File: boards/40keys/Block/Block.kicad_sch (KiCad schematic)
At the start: 196 parts, among them J1 Conn_01x08_Female, J1 Conn_01x12_Female, J2 Conn_01x12_Female, J3 Conn_01x12_Female, J4 Conn_01x08_Female, J6 Conn_01x12_Female, SW1 SW_Push, SW10 SW_Push, SW11 SW_Push, SW12 SW_Push, SW13 SW_Push, SW14 SW_Push, SW15 SW_Push, SW16 SW_Push, SW17 SW_Push, SW18 SW_Push, SW19 SW_Push, SW2 SW_Push, SW20 SW_Push, SW21 SW_Push, SW22 SW_Push, SW23 SW_Push, SW24 SW_Push, SW25 SW_Push, SW26 SW_Push, SW27 SW_Push, SW28 SW_Push, SW29 SW_Push, SW3 SW_Push, SW30 SW_Push, SW31 SW_Push, SW32 SW_Push, SW33 SW_Push, SW34 SW_Push, SW35 SW_Push, SW36 RotaryEncoder, SW36 Rotary_Encoder_Switch, SW37 SW_SPDT, SW38 SW_Push, SW39 SW_Push, SW4 SW_Push, SW40 SW_Push, SW41 SW_Push, SW42 SW_Push, SW43 SW_Push, SW44 SW_Push, SW45 SW_Push, SW46 SW_Push, SW5 SW_Push, SW6 SW_Push, SW7 SW_Push, SW8 SW_Push, SW9 SW_Push, U1 Elite-C, U2 74HC595, U3 TCR2EF19,LM(CT, U4 PMW3360DM-T2QU, U5 DRV2605L, U6 74LVC1T45

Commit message: block routed and jlc files
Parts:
- removed JP2: SolderJumper_3_Open, Jumper:SolderJumper-3_P1.3mm_Open_RoundedPad1.0x1.5mm_NumberLabels, symbol Jumper:SolderJumper_3_Open
- D1, D10, D11, D12, D13, D14, D15, D16, D17, D18, D19, D2, D20, D21, D22, D23, D24, D25, D26, D27, D28, D29, D3, D30, D31, D32, D33, D34, D4, D43, D5, D6, D7, D75, D76, D77, D78, D79, D8, D80, D81, D82, D9: footprint Diode_SMD:D_SOD-123 -> Alaa:D_SOD-123-rotated
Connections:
- net GPIO27 is gone; now on net EncR_1: U1.18 (A1/PF6)
- net GPIO16: now also JP3.2 (C)
- net LED_3V3: now also U1.28 (F1)
- net MOTION: now also JP3.3 (B); no longer U1.28 (F1)
- net NCS_2: now also U1.13 (10/PB6); no longer JP3.3 (B)
- removed net GPIO15: JP3.2 (C), U1.13 (10/PB6)

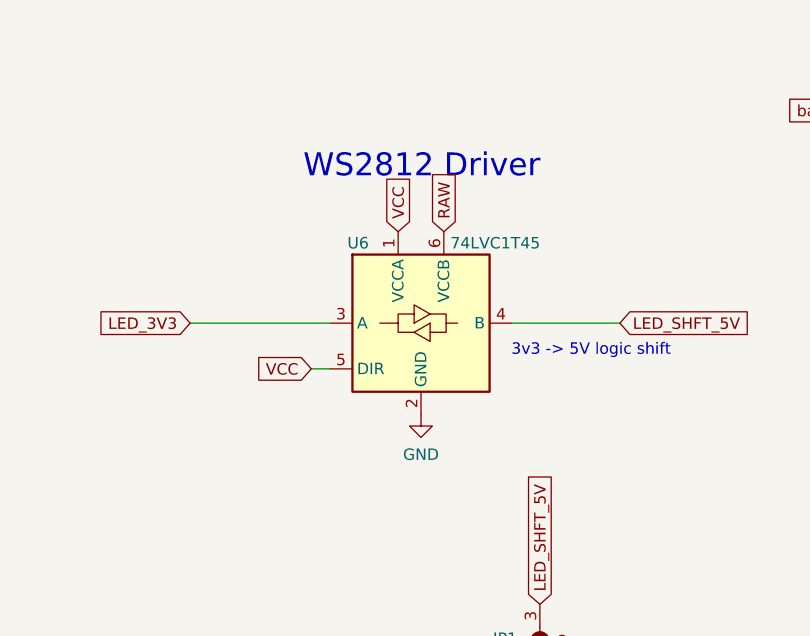
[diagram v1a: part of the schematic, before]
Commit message: block updated level shifter
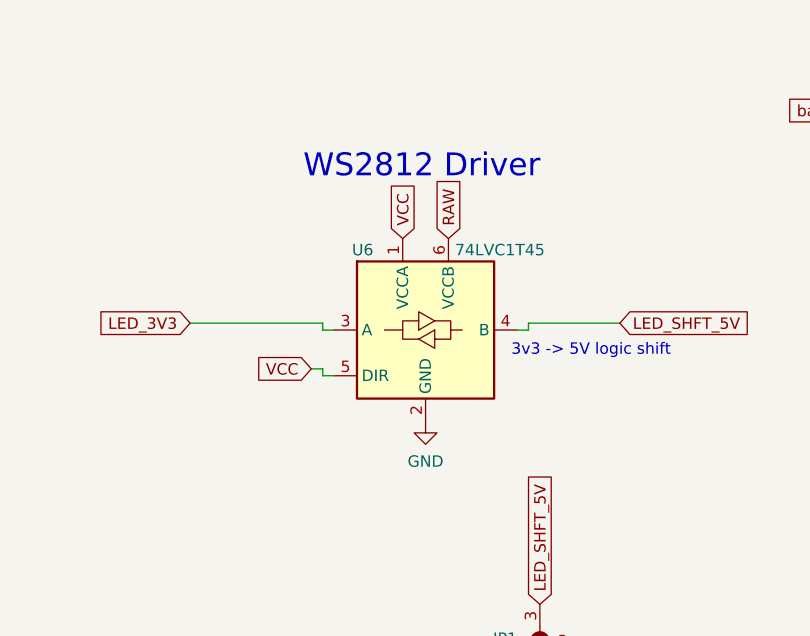
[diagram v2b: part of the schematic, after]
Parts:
- U6: footprint Package_TO_SOT_SMD:SOT-363_SC-70-6 -> Alaa:SOT-563; LCSC C139353 -> C352970
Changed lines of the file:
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@@
     (stroke (width 0) (type default))
   )
+  (wire (pts (xy 339.09 232.41) (xy 339.09 231.648))
+    (stroke (width 0) (type default))
+  )
   (wire (pts (xy 99.06 87.376) (xy 114.3 87.376))
     (stroke (width 0) (type default))
@@
     (stroke (width 0) (type default))
   )
-  (wire (pts (xy 337.312 231.648) (xy 349.25 231.648))
+  (wire (pts (xy 337.82 232.41) (xy 339.09 232.41))
     (stroke (width 0) (type default))
   )
@@
     (stroke (width 0) (type default))
   )
-  (wire (pts (xy 301.498 231.648) (xy 316.992 231.648))
+  (wire (pts (xy 316.23 232.41) (xy 317.5 232.41))
     (stroke (width 0) (type default))
   )
@@
     (stroke (width 0) (type default))
   )
+  (wire (pts (xy 339.09 231.648) (xy 349.25 231.648))
+    (stroke (width 0) (type default))
+  )
   (wire (pts (xy 471.17 311.15) (xy 486.41 311.15))
     (stroke (width 0) (type default))
@@
     (stroke (width 0) (type default))
   )
+  (wire (pts (xy 316.23 237.49) (xy 316.23 236.728))
+    (stroke (width 0) (type default))
+  )
   (wire (pts (xy 439.42 217.17) (xy 439.42 198.12))
     (stroke (width 0) (type default))
@@
     (stroke (width 0) (type default))
   )
+  (wire (pts (xy 316.23 232.41) (xy 316.23 231.648))
+    (stroke (width 0) (type default))
+  )
   (wire (pts (xy 96.52 78.74) (xy 96.52 105.156))
     (stroke (width 0) (type default))
@@
     (stroke (width 0) (type default))
   )
-  (wire (pts (xy 314.96 236.728) (xy 316.992 236.728))
+  (wire (pts (xy 316.23 237.49) (xy 317.5 237.49))
     (stroke (width 0) (type default))
   )
@@
     (stroke (width 0) (type default))
   )
+  (wire (pts (xy 316.23 231.648) (xy 301.498 231.648))
+    (stroke (width 0) (type default))
+  )
   (wire (pts (xy 96.52 184.15) (xy 96.52 158.75))
     (stroke (width 0) (type default))
@@
     (stroke (width 0) (type default))
   )
+  (wire (pts (xy 316.23 236.728) (xy 314.96 236.728))
+    (stroke (width 0) (type default))
+  )
   (wire (pts (xy 448.31 200.66) (xy 538.48 200.66))
     (stroke (width 0) (type default))
@@
     )
   )
-  (global_label "VCC" (shape input) (at 324.612 221.488 90) (fields_autoplaced)
+  (global_label "VCC" (shape input) (at 325.12 222.25 90) (fields_autoplaced)
     (effects (font (size 1.27 1.27)) (justify left))
-    (property "Intersheetrefs" "${INTERSHEET_REFS}" (at 324.5326 215.4463 90)
+    (property "Intersheetrefs" "${INTERSHEET_REFS}" (at 325.0406 216.2083 90)
       (effects (font (size 1.27 1.27)) (justify left) hide)
     )
@@
     )
   )
-  (global_label "RAW" (shape input) (at 329.692 221.488 90) (fields_autoplaced)
+  (global_label "RAW" (shape input) (at 330.2 222.25 90) (fields_autoplaced)
     (effects (font (size 1.27 1.27)) (justify left))
-    (property "Intersheetrefs" "${INTERSHEET_REFS}" (at 329.6126 215.2649 90)
+    (property "Intersheetrefs" "${INTERSHEET_REFS}" (at 330.1206 216.0269 90)
       (effects (font (size 1.27 1.27)) (justify left) hide)
     )
@@
     )
   )
-  (symbol (lib_id "Logic_LevelTranslator:SN74LVC1T45DRL") (at 327.152 231.648 0) (unit 1)
-    (in_bom yes) (on_board yes) (dnp no)
-    (property "Reference" "U6" (at 320.167 222.758 0)
-      (effects (font (size 1.27 1.27)))
-    )
-    (property "Value" "74LVC1T45" (at 335.407 222.758 0)
-      (effects (font (size 1.27 1.27)))
-    )
-    (property "Footprint" "Package_TO_SOT_SMD:SOT-363_SC-70-6" (at 327.152 243.078 0)
-      (effects (font (size 1.27 1.27)) hide)
-    )
-    (property "Datasheet" "" (at 304.292 248.158 0)
-      (effects (font (size 1.27 1.27)) hide)
-    )
-    (property "JLC Basic" "N" (at 327.152 231.648 0)
-      (effects (font (size 1.27 1.27)) hide)
-    )
-    (property "LCSC" "C139353" (at 327.152 231.648 0)
-      (effects (font (size 1.27 1.27)) hide)
-    )
-    (property "MPN " "SN74LVC1T45DRLR" (at 327.152 231.648 0)
-      (effects (font (size 1.27 1.27)) hide)
-    )
-    (property "Manufacturer" "Texas Instruments" (at 327.152 231.648 0)
-      (effects (font (size 1.27 1.27)) hide)
-    )
-    (property "Substitute" "N" (at 327.152 231.648 0)
-      (effects (font (size 1.27 1.27)) hide)
-    )
-    (pin "1")
-    (pin "2")
-    (pin "3")
-    (pin "4")
-    (pin "5")
-    (pin "6")
-    (instances
-      (project "Block"
-        (path "/eaef1172-3351-417c-bfc4-74a598f141cb"
-          (reference "U6") (unit 1)
-        )
-      )
-    )
-  )
   (symbol (lib_id "power:GND") (at 311.658 159.512 180) (unit 1)
     (in_bom yes) (on_board yes) (dnp no)
@@
     )
   )
+  (symbol (lib_id "Logic_LevelTranslator:SN74LVC1T45DRL") (at 327.66 232.41 0) (unit 1)
+    (in_bom yes) (on_board yes) (dnp no)
+    (property "Reference" "U6" (at 320.675 223.52 0)
+      (effects (font (size 1.27 1.27)))
+    )
+    (property "Value" "74LVC1T45" (at 335.915 223.52 0)
+      (effects (font (size 1.27 1.27)))
+    )
+    (property "Footprint" "Alaa:SOT-563" (at 327.66 243.84 0)
+      (effects (font (size 1.27 1.27)) hide)
+    )
+    (property "Datasheet" "" (at 304.8 248.92 0)
+      (effects (font (size 1.27 1.27)) hide)
+    )
+    (property "JLC Basic" "N" (at 327.66 232.41 0)
+      (effects (font (size 1.27 1.27)) hide)
+    )
+    (property "LCSC" "C352970" (at 327.66 232.41 0)
+      (effects (font (size 1.27 1.27)) hide)
+    )
+    (property "MPN " "SN74LVC1T45DRLR" (at 327.66 232.41 0)
+      (effects (font (size 1.27 1.27)) hide)
+    )
+    (property "Manufacturer" "Texas Instruments" (at 327.66 232.41 0)
+      (effects (font (size 1.27 1.27)) hide)
+    )
+    (property "Substitute" "N" (at 327.66 232.41 0)
+      (effects (font (size 1.27 1.27)) hide)
+    )
+    (pin "1")
+    (pin "2")
+    (pin "3")
+    (pin "4")
+    (pin "5")
+    (pin "6")
+    (instances
+      (project "Block"
+        (path "/eaef1172-3351-417c-bfc4-74a598f141cb"
+          (reference "U6") (unit 1)
+        )
+      )
+    )
+  )
   (symbol (lib_id "Switch:SW_Push") (at 43.18 44.45 0) (unit 1)
     (in_bom yes) (on_board yes) (dnp no)
@@
     )
   )
-  (symbol (lib_id "power:GND") (at 327.152 241.808 0) (unit 1)
+  (symbol (lib_id "power:GND") (at 327.66 242.57 0) (unit 1)
     (in_bom yes) (on_board yes) (dnp no) (fields_autoplaced)
-    (property "Reference" "#PWR0106" (at 327.152 248.158 0)
+    (property "Reference" "#PWR0106" (at 327.66 248.92 0)
       (effects (font (size 1.27 1.27)) hide)
     )
-    (property "Value" "GND" (at 327.152 246.253 0)
+    (property "Value" "GND" (at 327.66 247.015 0)
       (effects (font (size 1.27 1.27)))
     )
-    (property "Footprint" "" (at 327.152 241.808 0)
+    (property "Footprint" "" (at 327.66 242.57 0)
       (effects (font (size 1.27 1.27)) hide)
     )
-    (property "Datasheet" "" (at 327.152 241.808 0)
+    (property "Datasheet" "" (at 327.66 242.57 0)
       (effects (font (size 1.27 1.27)) hide)
     )

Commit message: block case
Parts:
- U3: value TCR2EF19,LM(CT -> VRH1902LTX; LCSC C146366 -> VRH1902LTX
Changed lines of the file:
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@@
       (effects (font (size 1.27 1.27)))
     )
-    (property "Value" "TCR2EF19,LM(CT" (at 304.546 42.672 0)
+    (property "Value" "VRH1902LTX" (at 304.546 42.672 0)
       (effects (font (size 1.27 1.27)))
     )
@@
       (effects (font (size 1.27 1.27) italic) hide)
     )
-    (property "Datasheet" "http://www.ti.com/lit/ds/symlink/tlv700.pdf" (at 304.546 50.292 0)
+    (property "Datasheet" "" (at 304.546 50.292 0)
       (effects (font (size 1.27 1.27)) hide)
     )
-    (property "LCSC" "C146366" (at 304.546 51.562 0)
+    (property "LCSC" "VRH1902LTX" (at 304.546 51.562 0)
       (effects (font (size 1.27 1.27)) hide)
     )
